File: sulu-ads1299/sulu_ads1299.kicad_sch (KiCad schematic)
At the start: 45 parts, among them J1 Conn_01x08, J2 Conn_01x02, J3 Conn_02x05_Odd_Even, SW1 SW_DIP_x02, U1 TPS62222DDCT, U2 TLV71311PDBV, U3 LM2775DSG

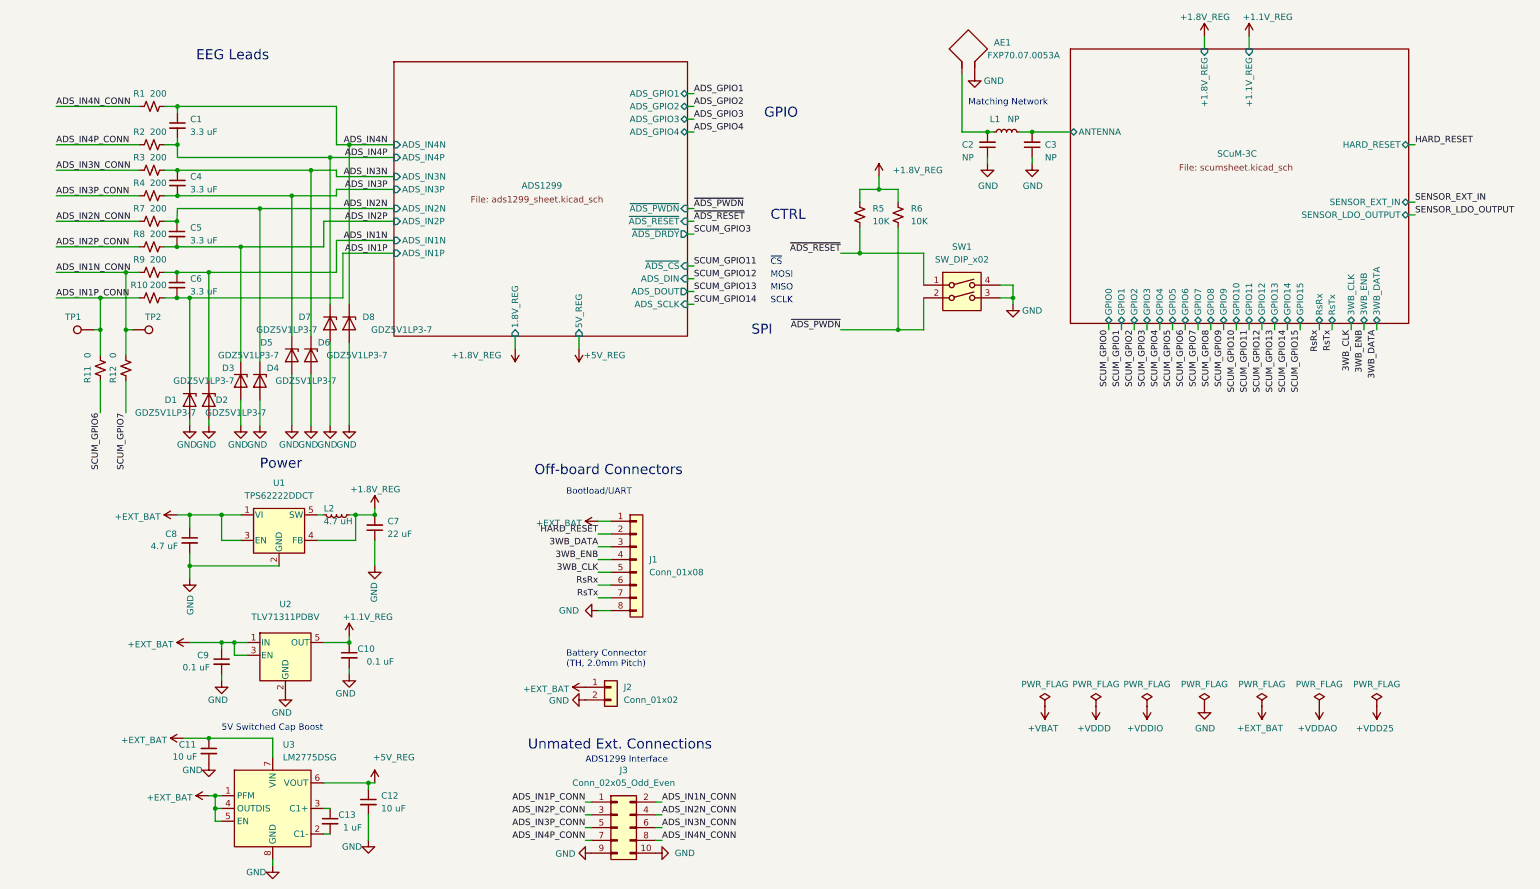
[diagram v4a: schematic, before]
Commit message: Updated connector boards and Sulu-ADS1299 schematic
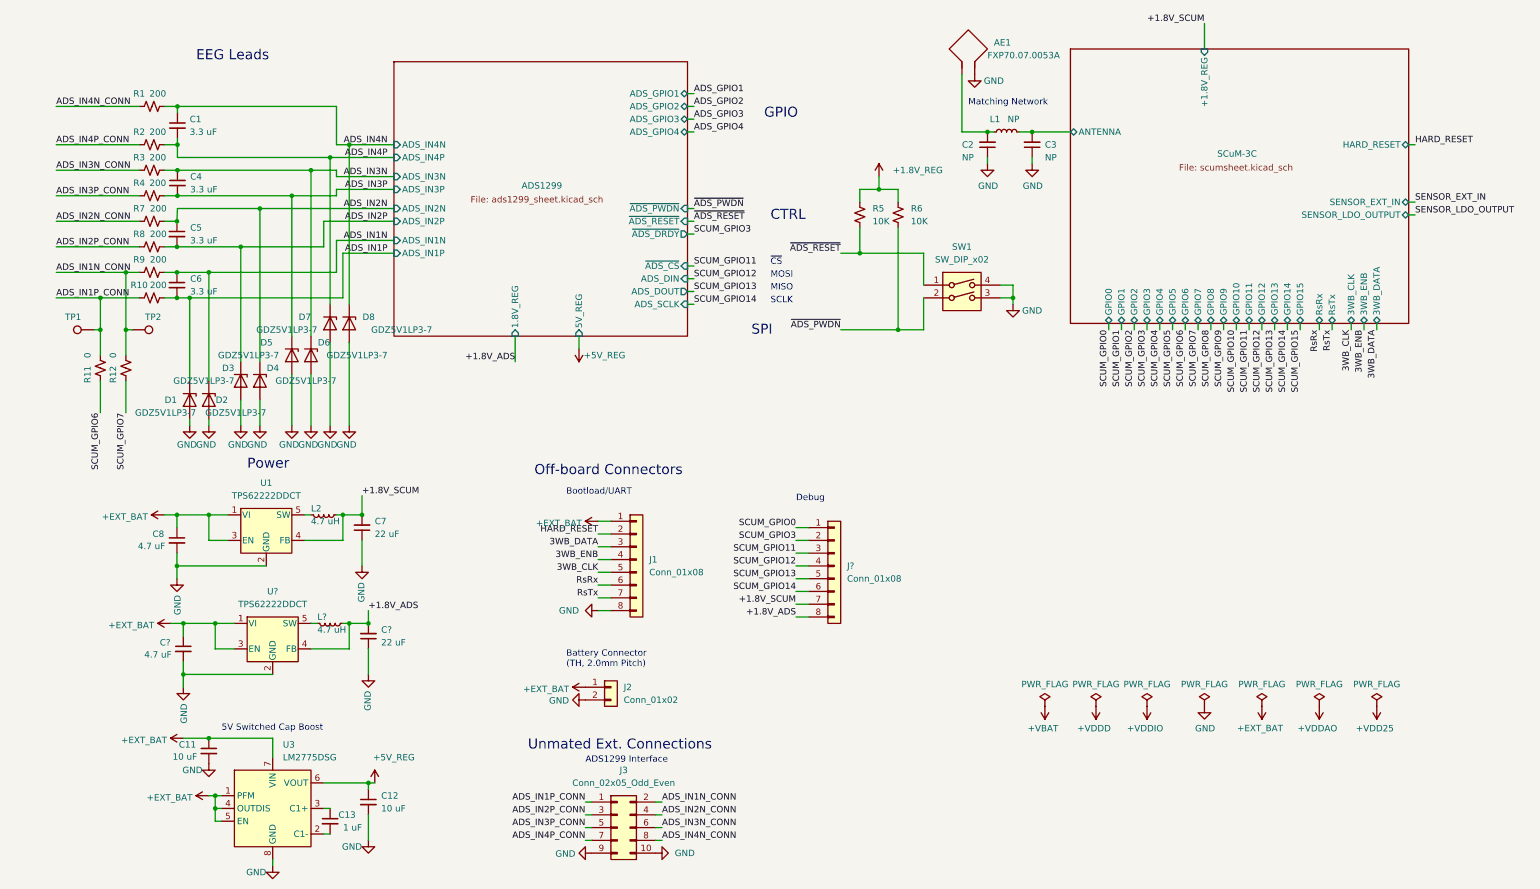
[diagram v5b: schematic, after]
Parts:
- removed C10, C9: 0.1 uF, Capacitor_SMD:C_0402_1005Metric, symbol Device:C_Small
- removed U2: TLV71311PDBV, Package_TO_SOT_SMD:SOT-23-5, symbol Regulator_Linear:TLV71311PDBV
- added C?: 22 uF, Capacitor_SMD:C_0603_1608Metric, symbol Device:C_Small
- added C?: 4.7 uF, Capacitor_SMD:C_0402_1005Metric, symbol Device:C_Small
- added J?: Conn_01x08, Molex Connectors:Molex_PicoBlade_53047-0810_1x08_P1.25mm_Vertical, symbol Connector_Generic:Conn_01x08
- added L?: 4.7 uH, Inductor_SMD:L_Wuerth_MAPI-2010, symbol Device:L_Small
- added U?: TPS62222DDCT, Package_TO_SOT_SMD:SOT-23-5, symbol draft1library:TPS62222DDCT
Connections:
- net +1.8V_REG: no longer C7.2, L2.1, U1.4 (FB)
- net +EXT_BAT: now also C?.1, U?.1 (VI), U?.3 (EN)
- net GND: now also C?.1, C?.2, U?.2 (GND)
- net SCUM_GPIO0: now also J?.1 (Pin_1)
- net SCUM_GPIO11: now also J?.3 (Pin_3)
- net SCUM_GPIO12: now also J?.4 (Pin_4)
- net SCUM_GPIO13: now also J?.5 (Pin_5)
- net SCUM_GPIO14: now also J?.6 (Pin_6)
- net SCUM_GPIO3: now also J?.2 (Pin_2)
- new net: L?.2, U?.5 (SW)
- new net +1.8V_ADS: C?.2, J?.8 (Pin_8), L?.1, U?.4 (FB)
- new net +1.8V_SCUM: C7.2, J?.7 (Pin_7), L2.1, U1.4 (FB)
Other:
- sheet SCuM-3C ports: added none; removed +1.1V_REG
- note added: "Debug"
- moved on the sheet: C7, C8, L2, U1

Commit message: Sulu-ADS1299 rev 3 fixed gpios, debug connector, two regulators
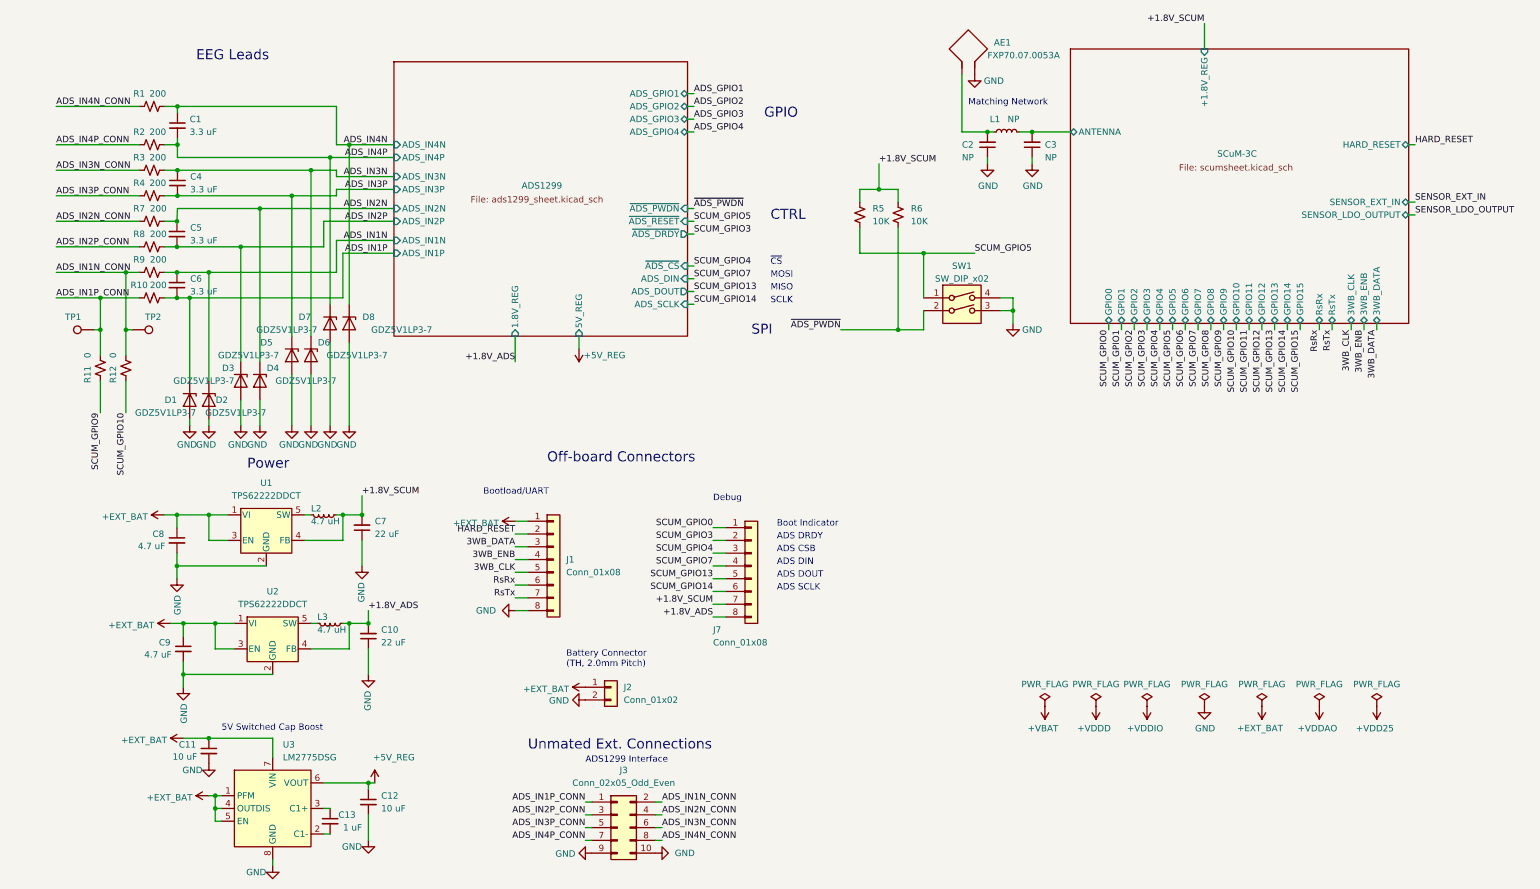
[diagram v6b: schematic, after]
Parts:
- D1, D2, D3, D4, D5, D6, D7, D8: footprint Diode_SMD:D_0201_0603Metric -> Diode_SMD:D_0402_1005Metric
- gave numbers to parts that had none: 5
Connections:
- net +1.8V_REG is gone; now on net +1.8V_SCUM: R5.1, R6.1
- net ~{ADS_RESET} is gone; now on net SCUM_GPIO5: R5.2, SW1.1
- net SCUM_GPIO10: now also R12.1
- net SCUM_GPIO11: no longer J7.3 (Pin_3)
- net SCUM_GPIO12: no longer J7.4 (Pin_4)
- net SCUM_GPIO4: now also J7.3 (Pin_3)
- net SCUM_GPIO6: no longer R11.1
- net SCUM_GPIO7: now also J7.4 (Pin_4); no longer R12.1
- net SCUM_GPIO9: now also R11.1
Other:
- note added: "ADS CSB"
- note added: "ADS DIN"
- note added: "ADS DOUT"
- note added: "ADS DRDY"
- note added: "ADS SCLK"
- note added: "Boot Indicator"
- moved on the sheet: J1, J7, SW1

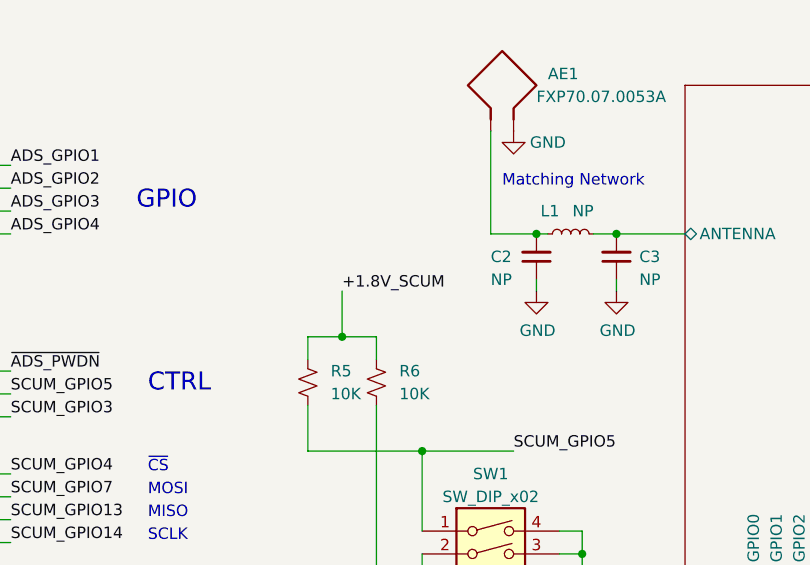
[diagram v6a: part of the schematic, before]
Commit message: Sulu-ADS1299 and connector board layout+sch progress
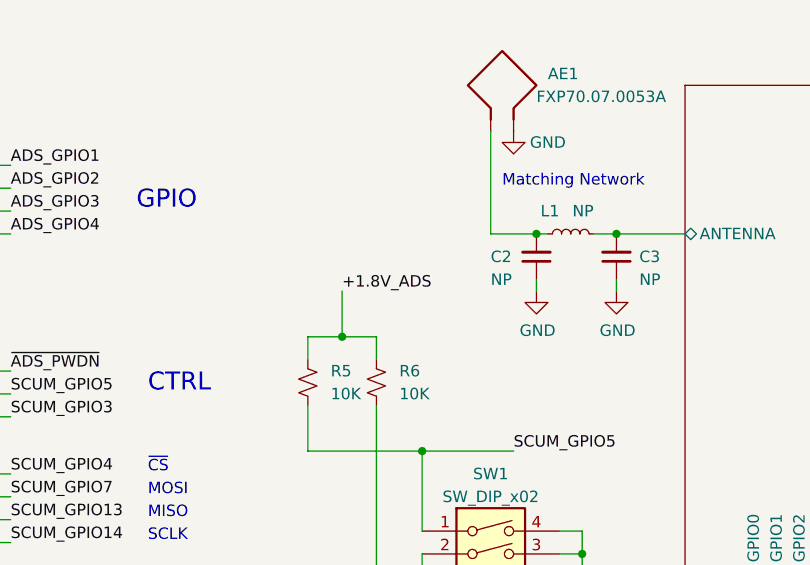
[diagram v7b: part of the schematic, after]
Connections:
- net +1.8V_ADS: now also R5.1, R6.1
- net +1.8V_SCUM: no longer R5.1, R6.1
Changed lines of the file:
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@@
     (effects (font (size 1.27 1.27)) (justify right bottom))
-  )
-  (label "+1.8V_SCUM" (at 176.53 43.18 0)
-    (effects (font (size 1.27 1.27)) (justify left bottom))
   )
   (label "SCUM_GPIO4" (at 232.41 76.2 270)
@@
   )
   (label "ADS_GPIO2" (at 139.7 31.75 0)
+    (effects (font (size 1.27 1.27)) (justify left bottom))
+  )
+  (label "+1.8V_ADS" (at 176.53 43.18 0)
     (effects (font (size 1.27 1.27)) (justify left bottom))
   )
@@
       (reference "#FLG07") (unit 1) (value "PWR_FLAG") (footprint "")
     )
-    (path "/1f92f92f-1391-4fc3-892c-7c652348c5b5/3e132f23-410c-4ce5-8e0f-c92f90b7c313"
-      (reference "#PWR01") (unit 1) (value "GND") (footprint "")
-    )
     (path "/0dcd86bf-94df-438f-a15a-b03787fe92a6"
       (reference "#PWR03") (unit 1) (value "GND") (footprint "")
@@
       (reference "J16") (unit 1) (value "through_hole") (footprint "SCUM:through_hole")
     )
-    (path "/1f92f92f-1391-4fc3-892c-7c652348c5b5/4ba82544-a1db-4898-96d3-bc5c8e39d339"
-      (reference "J17") (unit 1) (value "through_hole") (footprint "SCUM:through_hole")
-    )
     (path "/1f92f92f-1391-4fc3-892c-7c652348c5b5/b3a4ce07-043e-414d-9f6a-f264178ab753"
       (reference "J20") (unit 1) (value "through_hole") (footprint "SCUM:through_hole")
@@
       (reference "R14") (unit 1) (value "NP") (footprint "Resistor_SMD:R_0402_1005Metric")
     )
-    (path "/1f92f92f-1391-4fc3-892c-7c652348c5b5/59dbd52d-eaa1-4f9d-bb71-c0900f08ff23"
-      (reference "R15") (unit 1) (value "NP") (footprint "Resistor_SMD:R_0402_1005Metric")
+    (path "/1f92f92f-1391-4fc3-892c-7c652348c5b5/04c806ed-7196-4667-be22-85147aaf66e8"
+      (reference "RZ15") (unit 1) (value "0 Ohm") (footprint "Resistor_SMD:R_0402_1005Metric")
     )
     (path "/1bb106ea-ac1b-46fa-8465-e7cc217a10a6"

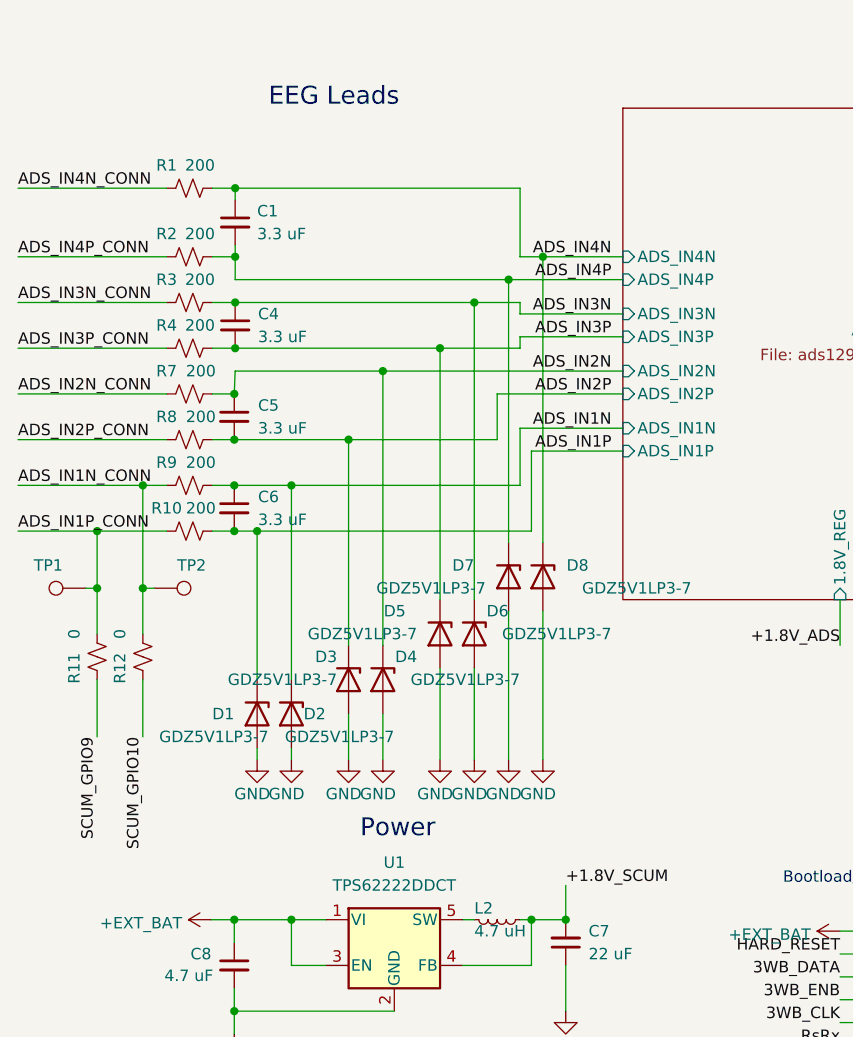
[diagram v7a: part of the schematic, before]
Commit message: Sulu-ADS1299 mosfet input protection circuit
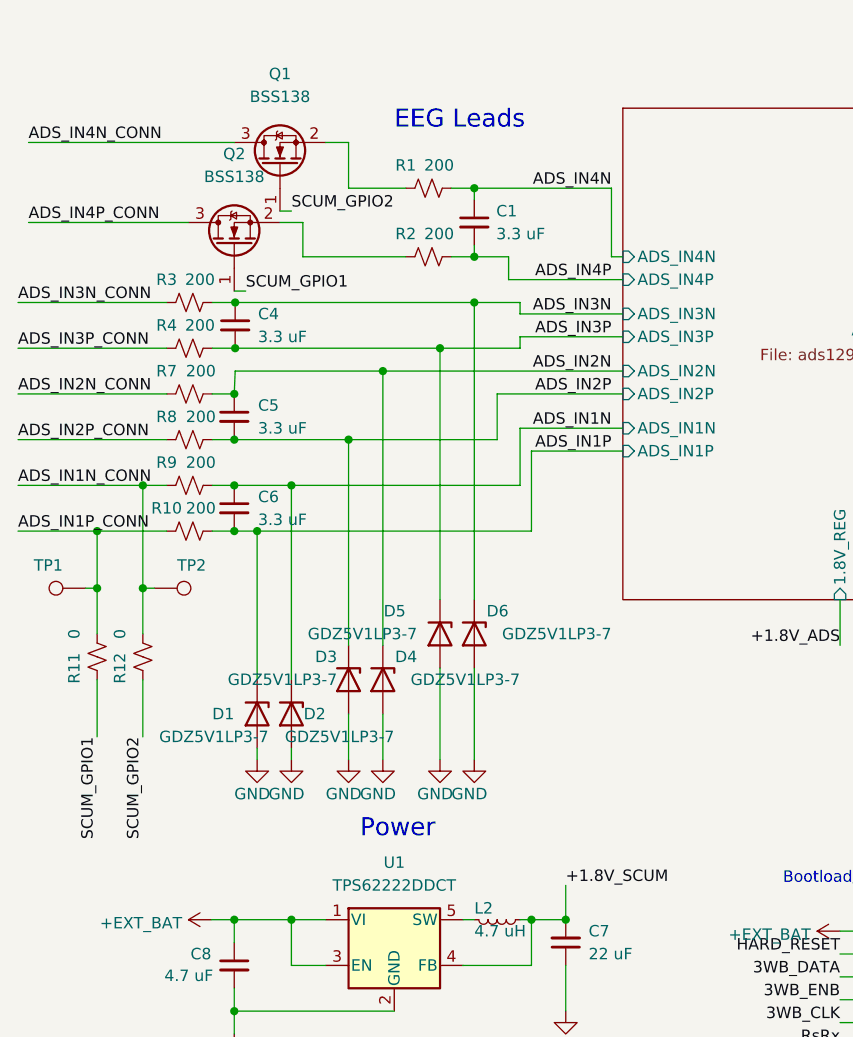
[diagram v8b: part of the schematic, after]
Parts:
- removed D7, D8: GDZ5V1LP3-7, Diode_SMD:D_0402_1005Metric, symbol Diode:BZV55B5V1
- added Q1, Q2: BSS138, Package_TO_SOT_SMD:SOT-23, symbol Transistor_FET:BSS138
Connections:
- net ADS_IN4N_CONN: now also Q1.3 (D); no longer R1.1
- net ADS_IN4P_CONN: now also Q2.3 (D); no longer R2.1
- net SCUM_GPIO1: now also R11.1, Q2.1 (G)
- net SCUM_GPIO10: no longer R12.1
- net SCUM_GPIO2: now also R12.1, Q1.1 (G)
- net SCUM_GPIO9: no longer R11.1
- new net: Q1.2 (S), R1.1
- new net: Q2.2 (S), R2.1
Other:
- moved on the sheet: C1, R1, R2
